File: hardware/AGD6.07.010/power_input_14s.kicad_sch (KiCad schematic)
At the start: 0 parts

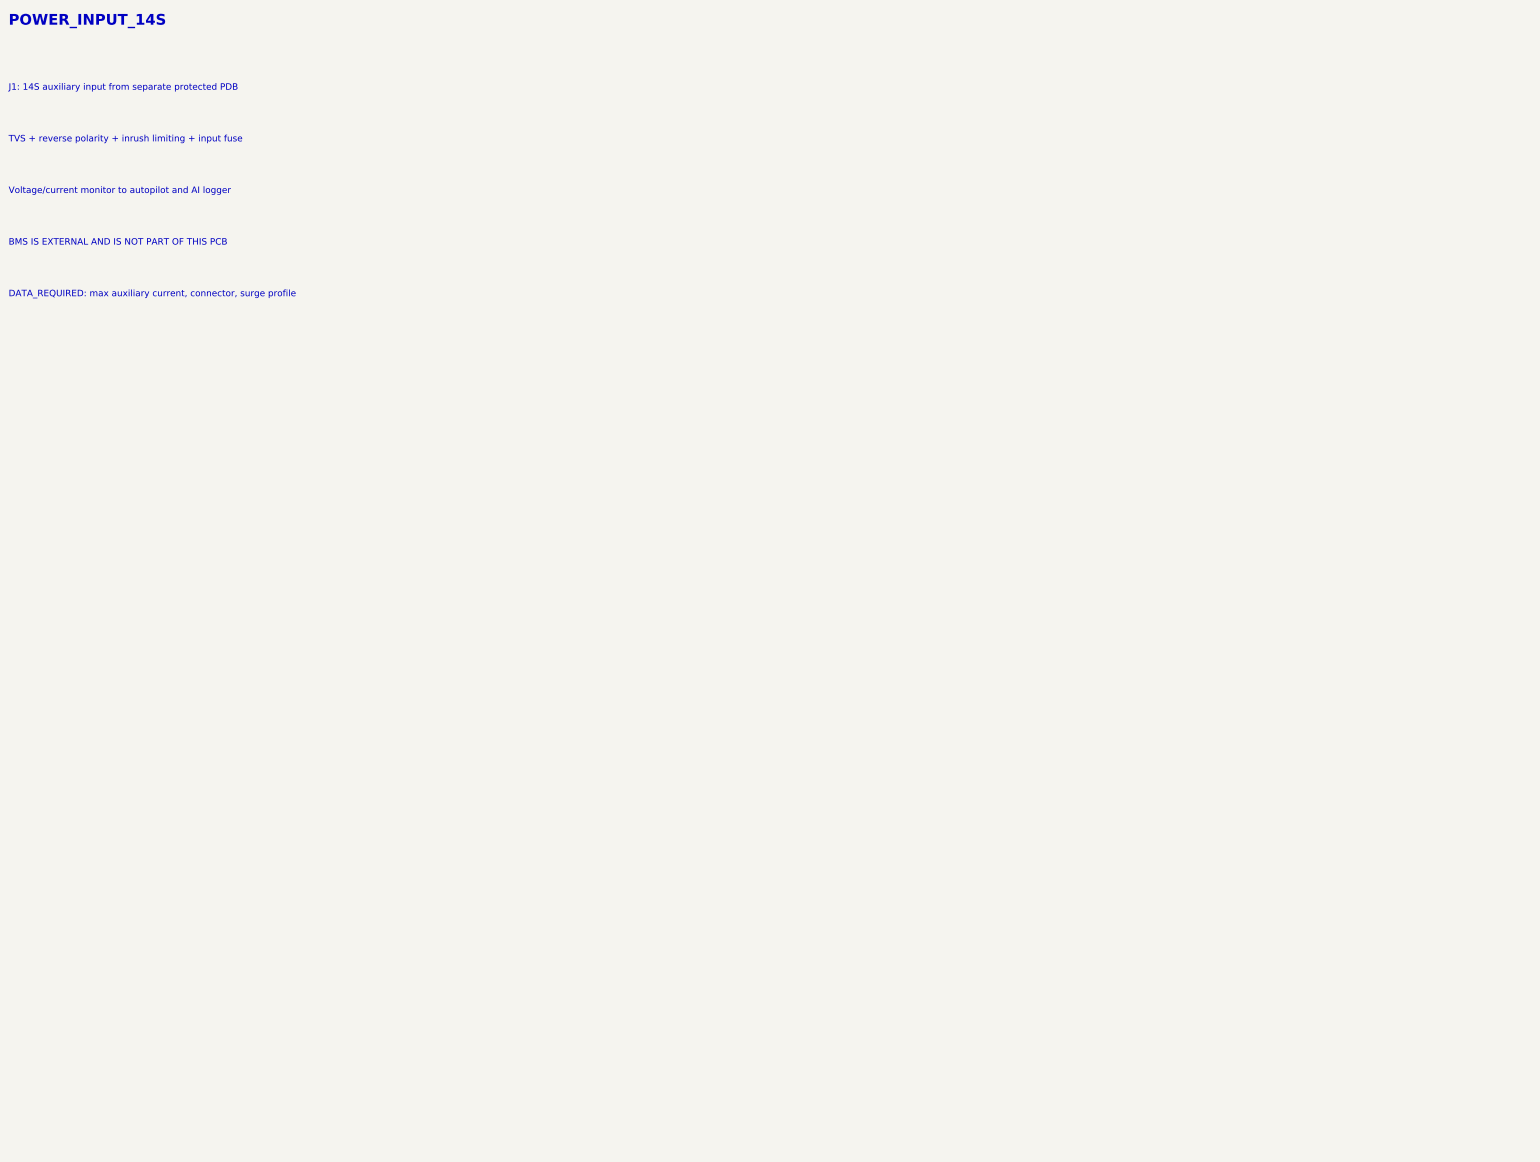
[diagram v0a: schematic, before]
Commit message: Draw full AGD6.07.010 schematic per integrated_avionics_board spec
All ten sheets now carry components: 14S input with hot-swap and power
monitor, 12/5/3.3 V rails and a separate 12 V AI channel with soft-start
and current telemetry, Pixhawk connectors, CAN1/CAN2 hub with chokes,
ESD and switchable termination, sensor conditioning, SIYI and radar,
AI interface and watchdog, protected 12 V switches with diagnostics,
fan/heater control, cameras and Ethernet. Open choices are recorded in
DECISIONS.md; datasheet-dependent values are flagged CHECK_DATASHEET.

ERC: no errors. All 752 intended pin connections match the KiCad netlist.

Co-Authored-By: Claude Opus 5.5 <noreply@anthropic.com>
Claude-Session: https://claude.ai/code/session_01Qk7uTKdi6YbndB9fGuguYV
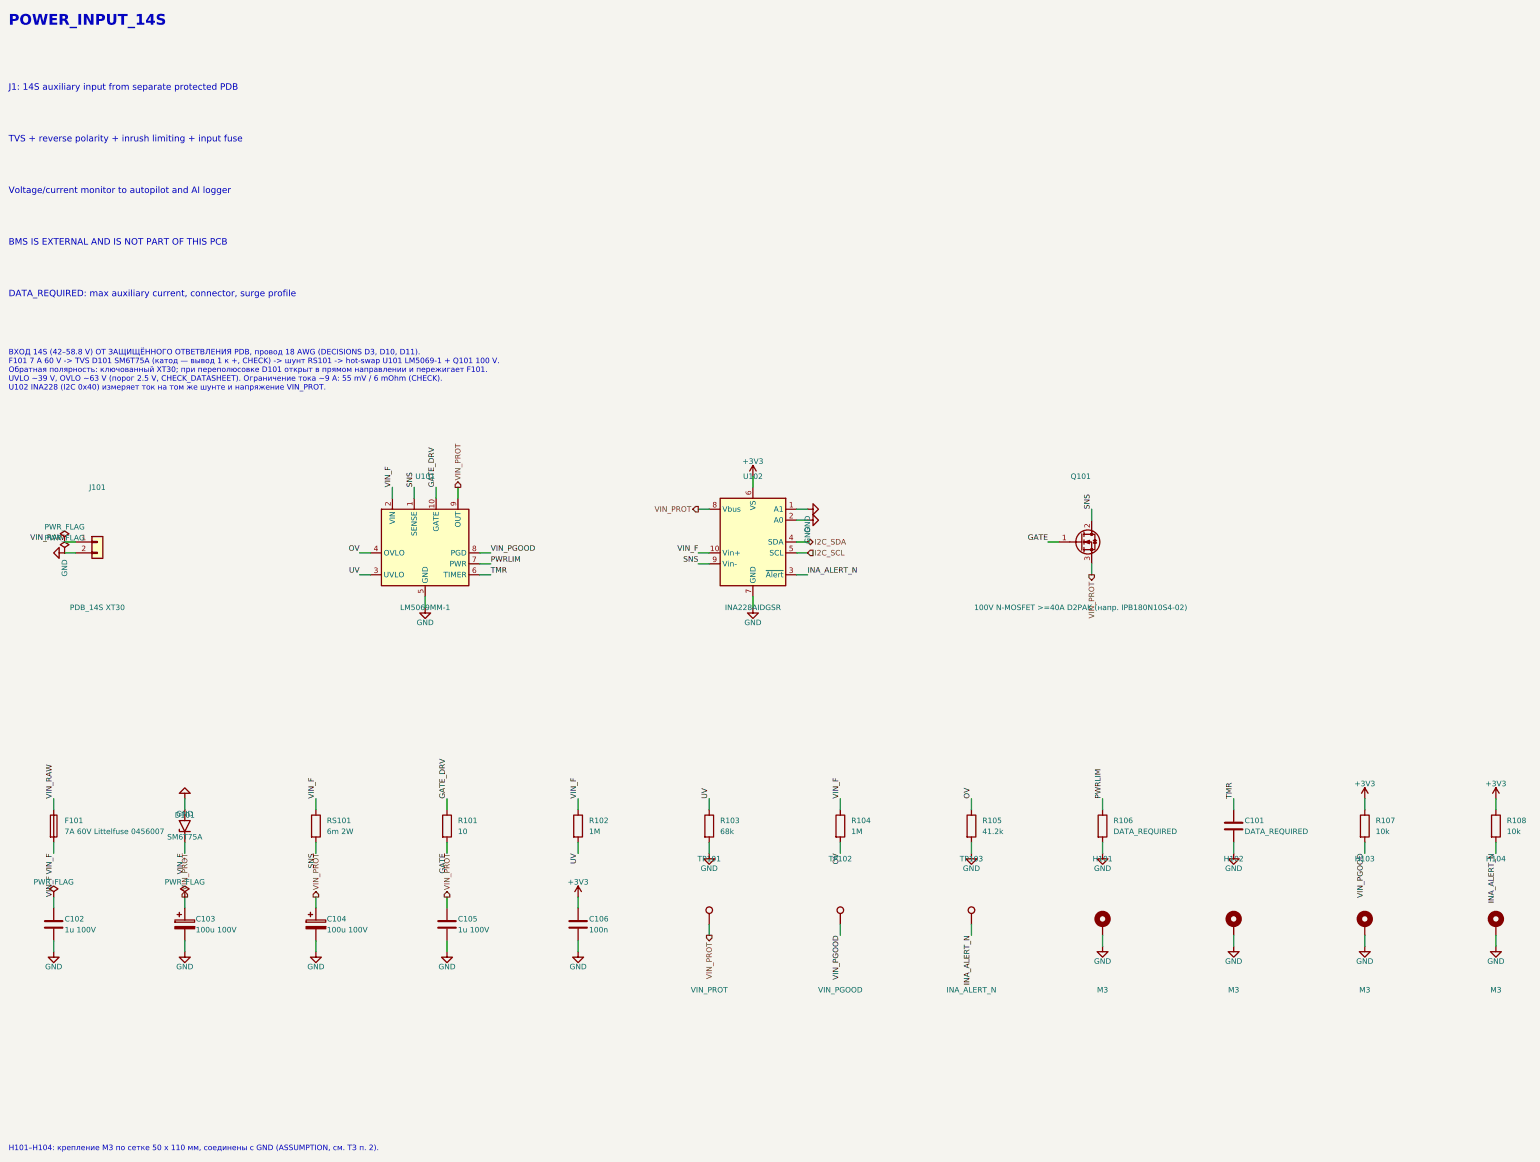
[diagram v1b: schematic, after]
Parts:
- added C101: DATA_REQUIRED, Capacitor_SMD:C_0402_1005Metric, symbol Device:C
- added C102, C105: 1u 100V, Capacitor_SMD:C_1210_3225Metric, symbol Device:C
- added C103, C104: 100u 100V, Capacitor_SMD:CP_Elec_10x10.5, symbol Device:C_Polarized
- added C106: 100n, Capacitor_SMD:C_0402_1005Metric, symbol Device:C
- added D101: SM6T75A, Diode_SMD:D_SMB, symbol Diode:SM6T75A
- added F101: 7A 60V Littelfuse 0456007, Fuse:Fuse_Littelfuse-NANO2-451_453, symbol Device:Fuse
- added H101, H102, H103, H104: M3, MountingHole:MountingHole_3.2mm_M3_Pad_Via, symbol Mechanical:MountingHole_Pad
- added J101: PDB_14S XT30, Connector_AMASS:AMASS_XT30PW-M_1x02_P2.50mm_Horizontal, symbol Connector_Generic:Conn_01x02
- added Q101: 100V N-MOSFET >=40A D2PAK (напр. IPB180N10S4-02), Package_TO_SOT_SMD:TO-263-2, symbol Transistor_FET:Q_NMOS_GDS
- added R101: 10, Resistor_SMD:R_0402_1005Metric, symbol Device:R
- added R102, R104: 1M, Resistor_SMD:R_0603_1608Metric, symbol Device:R
- added R103: 68k, Resistor_SMD:R_0603_1608Metric, symbol Device:R
- added R105: 41.2k, Resistor_SMD:R_0603_1608Metric, symbol Device:R
- added R106: DATA_REQUIRED, Resistor_SMD:R_0402_1005Metric, symbol Device:R
- added R107, R108: 10k, Resistor_SMD:R_0402_1005Metric, symbol Device:R
- added RS101: 6m 2W, Resistor_SMD:R_2512_6332Metric, symbol Device:R
- added TP101: VIN_PROT, TestPoint:TestPoint_Pad_D1.5mm, symbol Connector:TestPoint
- added TP102: VIN_PGOOD, TestPoint:TestPoint_Pad_D1.5mm, symbol Connector:TestPoint
- added TP103: INA_ALERT_N, TestPoint:TestPoint_Pad_D1.5mm, symbol Connector:TestPoint
- added U101: LM5069MM-1, Package_SO:MSOP-10_3x3mm_P0.5mm, symbol Power_Management:LM5069MM-1
- added U102: INA228AIDGSR, Package_SO:TSSOP-10_3x3mm_P0.5mm, symbol Sensor_Energy:INA228
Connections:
- new net +3V3: C106.1, R107.1, R108.1, U102.6 (VS)
- new net GATE: Q101.1 (G), R101.2
- new net GATE_DRV: R101.1, U101.10 (GATE)
- new net GND: C101.2, C102.2, C103.2, C104.2, C105.2, C106.2, D101.2 (A2), H101.1, H102.1, H103.1, H104.1, J101.2 (Pin_2), R103.2, R105.2, R106.2, U101.5 (GND), U102.1 (A1), U102.2 (A0), U102.7 (GND)
- new net I2C_SCL: U102.5 (SCL)
- new net I2C_SDA: U102.4 (SDA)
- new net INA_ALERT_N: R108.2, TP103.1, U102.3 (~{Alert})
- new net OV: R104.2, R105.1, U101.4 (OVLO)
- new net PWRLIM: R106.1, U101.7 (PWR)
- new net SNS: Q101.2 (D), RS101.2, U101.1 (SENSE), U102.9 (Vin-)
- new net TMR: C101.1, U101.6 (TIMER)
- new net UV: R102.2, R103.1, U101.3 (UVLO)
- new net VIN_F: C102.1, D101.1 (A1), F101.2, R102.1, R104.1, RS101.1, U101.2 (VIN), U102.10 (Vin+)
- new net VIN_PGOOD: R107.2, TP102.1, U101.8 (PGD)
- new net VIN_PROT: C103.1, C104.1, C105.1, Q101.3 (S), TP101.1, U101.9 (OUT), U102.8 (Vbus)
- new net VIN_RAW: F101.1, J101.1 (Pin_1)
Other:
- note added: "H101–H104: крепление M3 по сетке 50 x 110 мм, соединены с GND (ASSUMPTION, см. ТЗ п. 2)."
- note added: "ВХОД 14S (42–58.8 V) ОТ ЗАЩИЩЁННОГО ОТВЕТВЛЕНИЯ PDB, провод 18 AWG (DECISIONS D3, D10, D11). F101 7 A 60 V -> TVS D101 SM6T75A (катод — вывод 1 к +, CHECK) -> шунт RS101 -> hot-swap U101 LM5069-1 + Q101 100 V. Обратная полярность: ключованный XT30; при переполюсовке D101 открыт в прямом направлении и пережигает F101. UVLO ~39 V, OVLO ~63 V (порог 2.5 V, CHECK_DATASHEET). Ограничение тока ~9 A: 55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"
- company: (none) -> АГД6.07.010
- title: (none) -> POWER_INPUT_14S
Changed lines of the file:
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@@
-(kicad_sch
-	(version 20260306)
-	(generator "eeschema")
-	(generator_version "10.0")
-	(paper "A4")
-	(text "BMS IS EXTERNAL AND IS NOT PART OF THIS PCB"
-		(exclude_from_sim no)
-		(at 20 71 0)
-		(effects
-			(font
-				(size 1.5 1.5)
-			)
-			(justify left bottom)
-		)
-	)
-	(text "TVS + reverse polarity + inrush limiting + input fuse"
-		(exclude_from_sim no)
-		(at 20 47 0)
-		(effects
-			(font
-				(size 1.5 1.5)
-			)
-			(justify left bottom)
-		)
-	)
-	(text "POWER_INPUT_14S"
-		(exclude_from_sim no)
-		(at 20 20 0)
-		(effects
-			(font
-				(size 2.5 2.5)
-				(bold yes)
-			)
-			(justify left bottom)
-		)
-	)
-	(text "DATA_REQUIRED: max auxiliary current, connector, surge profile"
-		(exclude_from_sim no)
-		(at 20 83 0)
-		(effects
-			(font
-				(size 1.5 1.5)
-			)
-			(justify left bottom)
-		)
-	)
-	(text "Voltage/current monitor to autopilot and AI logger"
-		(exclude_from_sim no)
-		(at 20 59 0)
-		(effects
-			(font
-				(size 1.5 1.5)
-			)
-			(justify left bottom)
-		)
-	)
-	(text "J1: 14S auxiliary input from separate protected PDB"
-		(exclude_from_sim no)
-		(at 20 35 0)
-		(effects
-			(font
-				(size 1.5 1.5)
-			)
-			(justify left bottom)
-		)
-	)
-	(sheet_instances
-		(path "/"
-			(page "1")
-		)
-	)
-)

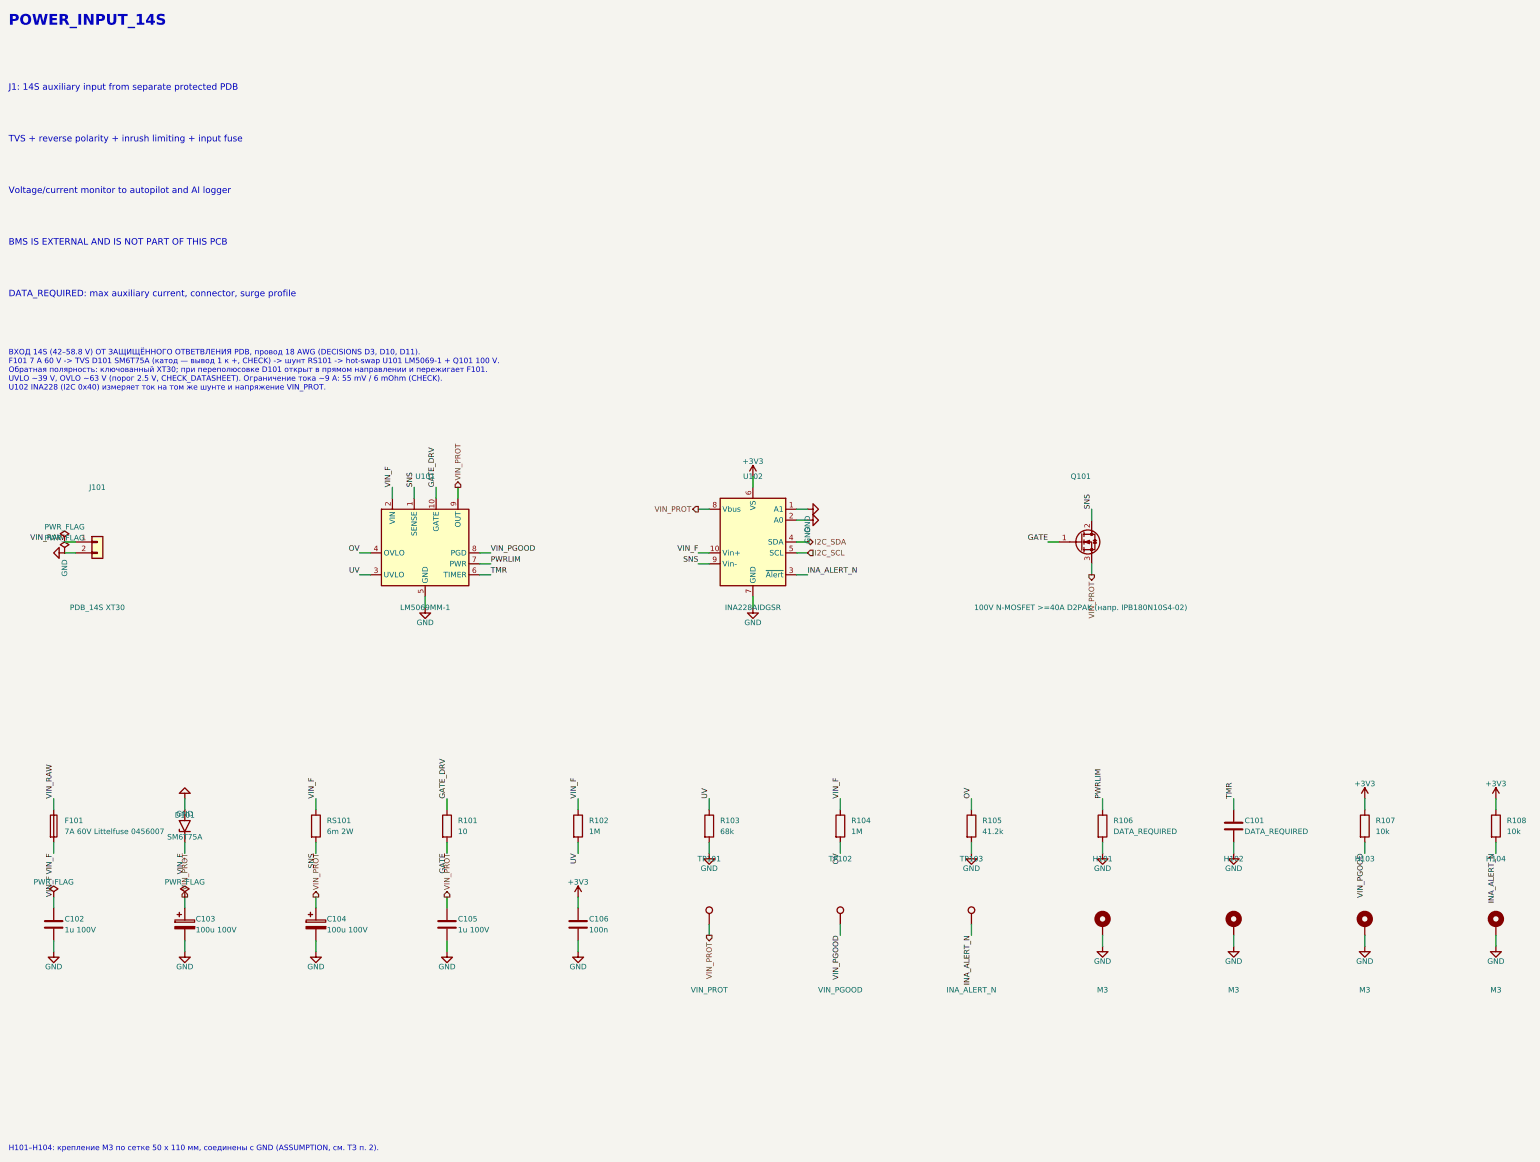
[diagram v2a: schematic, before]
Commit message: AGD6.07.010 rev 0.3: design review fixes and bring-up plan
Design review (DESIGN_REVIEW.md) with fixes applied to the schematic:
INA228 input RC filters, 12 V bus current monitor (INA228 0x45),
BTS5030 diagnostic scaling with clamp diodes, flow input level fix,
CAN1 changed from star to daisy chain with on-board terminator, AI
shutdown request, board buzzer, series resistors and ESD on external
I2C probes. Connectors merged so every connector sits on a board edge.
Adds calculations.md (power, IPC-2221 widths, hot-swap, thermal, ADC
scaling, CAN, clearances) and BRINGUP.md (step-by-step test plan).
ERC: no errors; all 820 intended pin connections verified. Board is
re-placed; routing in progress.

Co-Authored-By: Claude Opus 5.5 <noreply@anthropic.com>
Claude-Session: https://claude.ai/code/session_01Qk7uTKdi6YbndB9fGuguYV
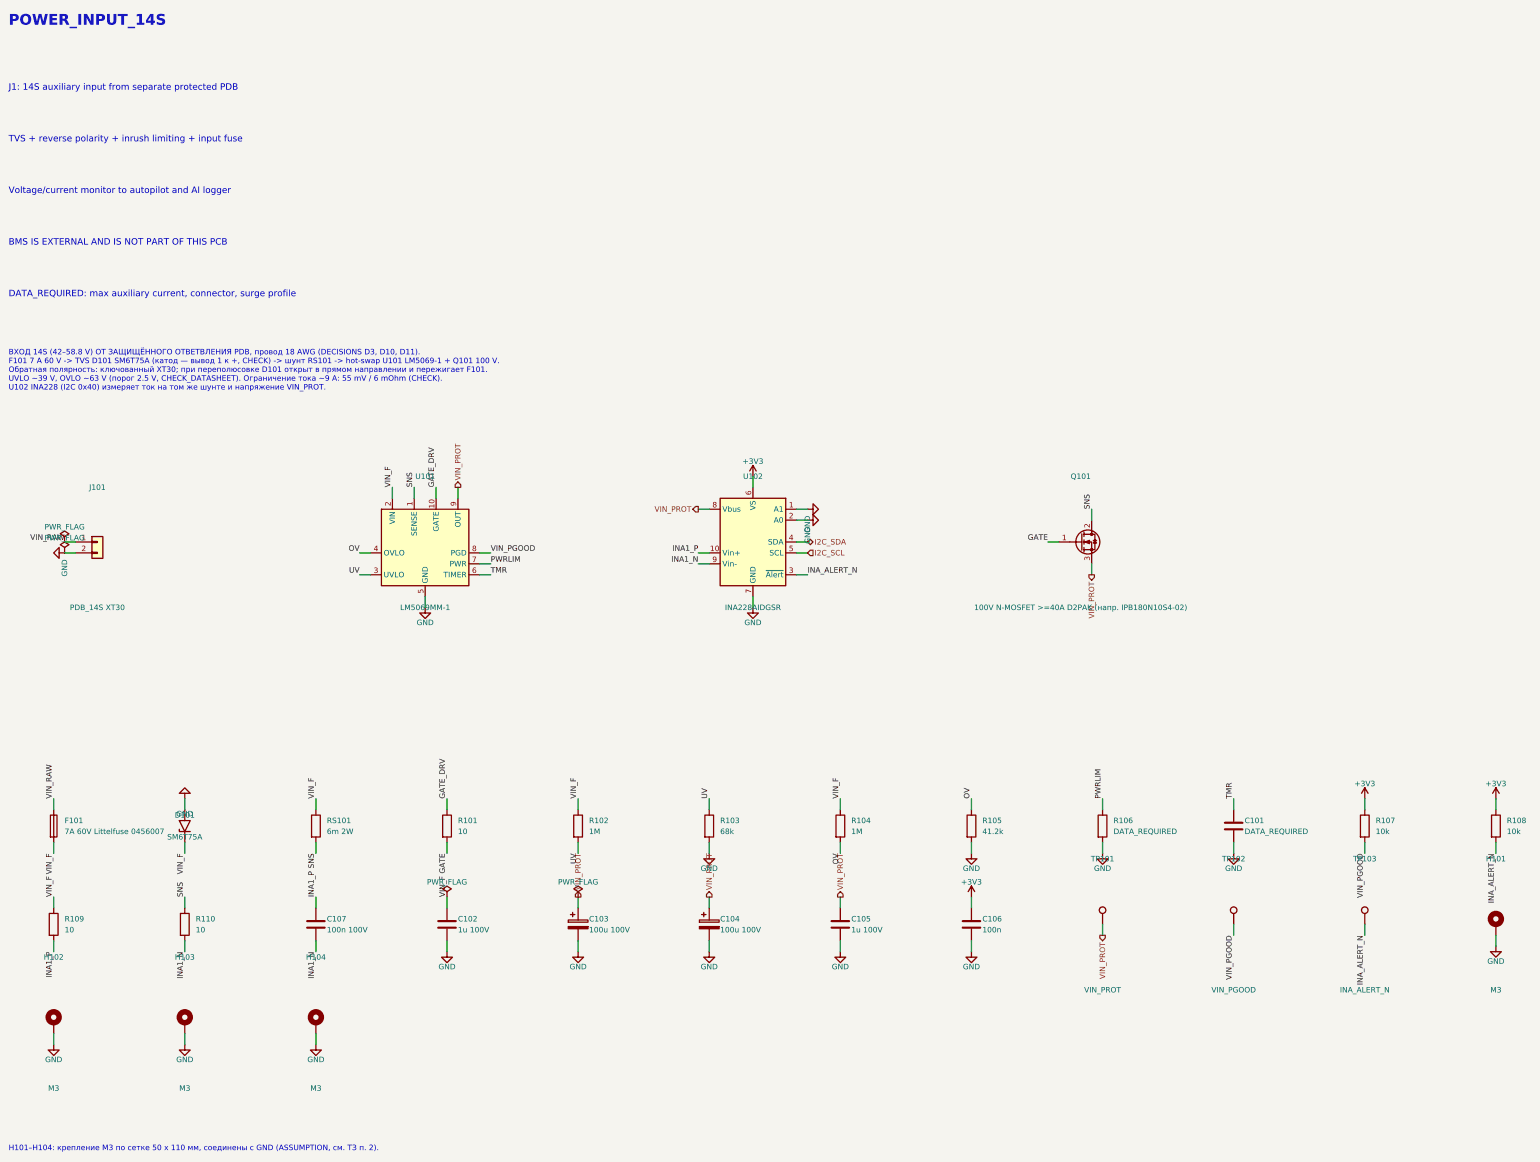
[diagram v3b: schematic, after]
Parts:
- added C107: 100n 100V, Capacitor_SMD:C_0603_1608Metric, symbol Device:C
- added R109, R110: 10, Resistor_SMD:R_0603_1608Metric, symbol Device:R
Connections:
- net SNS: now also R110.1; no longer U102.9 (Vin-)
- net VIN_F: now also R109.1; no longer U102.10 (Vin+)
- new net INA1_N: C107.2, R110.2, U102.9 (Vin-)
- new net INA1_P: C107.1, R109.2, U102.10 (Vin+)
